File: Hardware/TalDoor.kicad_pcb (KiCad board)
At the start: 2 copper layers, 117.2 x 60.3 mm, 72 parts, among them J1 SI-52003-F_RJ45, J2 Conn_01x02, J3 Conn_01x06_Male, J4 Conn_01x06_Male, M2 Screw MountingHole_2.2mm_M2_Pad_Via, P1 PocketBeagle, Q1 RK7002BM, Q2 BSS223PWH6327XTSA1, U1 DRV8837, U2 ENC28J60-I/SO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

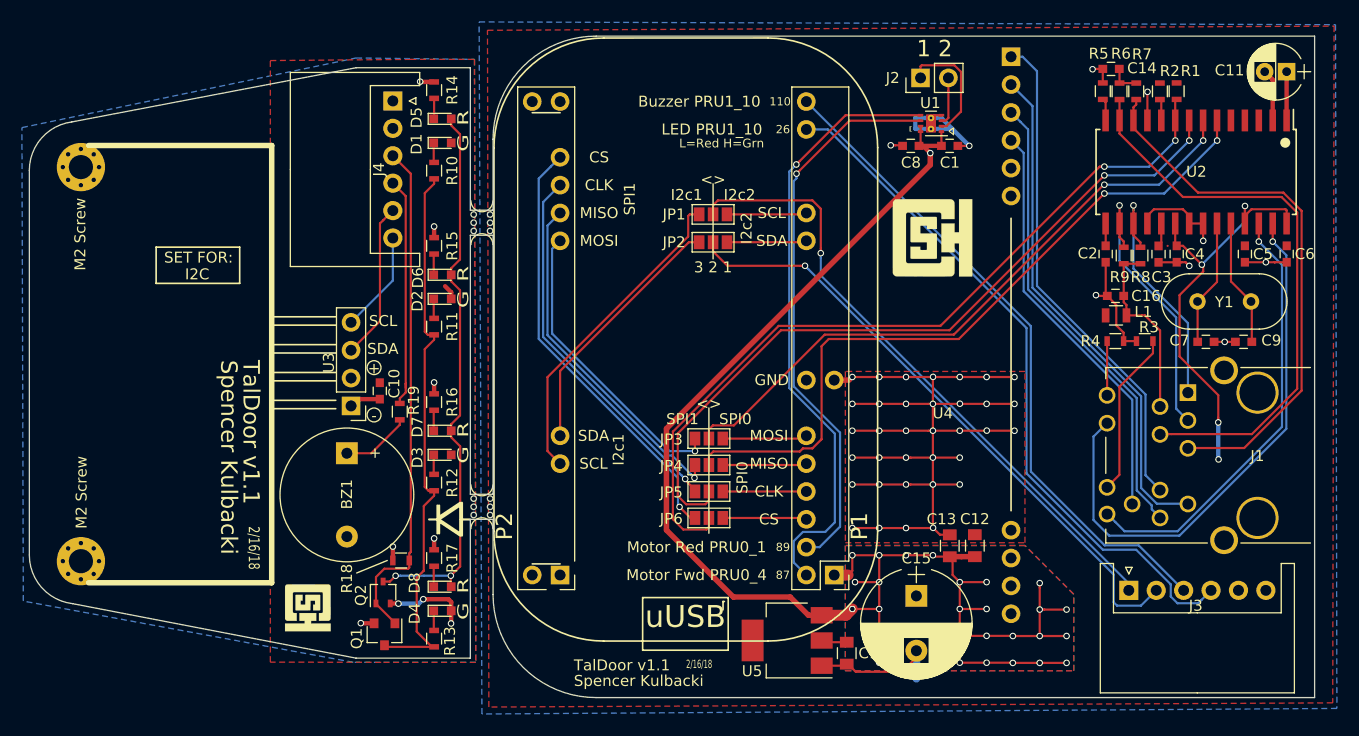
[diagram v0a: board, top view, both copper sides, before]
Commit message: updated layout to account for door mount shape issue
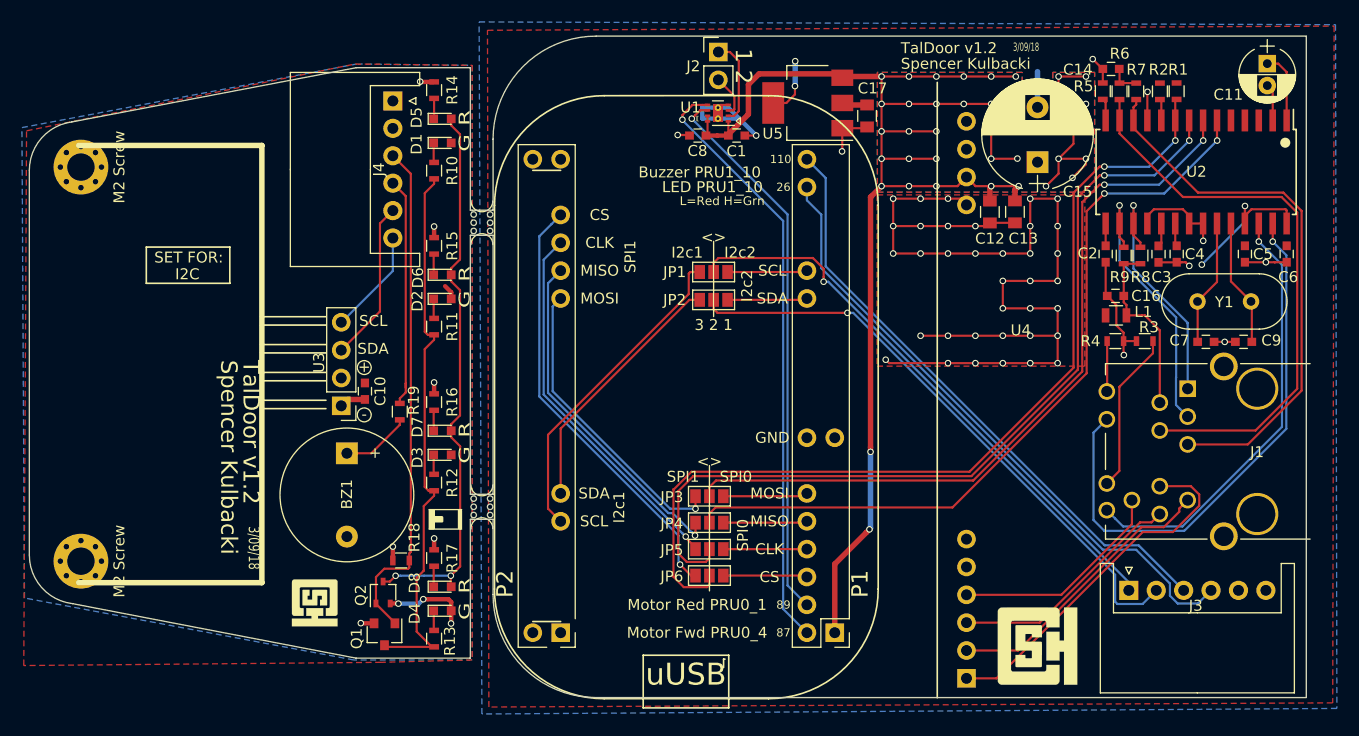
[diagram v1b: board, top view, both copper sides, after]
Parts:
- M2 Screw: footprint Mounting_Holes:MountingHole_2.2mm_M2_Pad_Via -> Mounting_Holes:MountingHole_2.5mm_Pad_Via (x2)
- moved U4 61.0 mm to (139.3, 163.5), turned to 180 degrees
- moved U5 49.1 mm to (127.5, 109.2)
- moved C17 49.0 mm to (132.9, 110.4)
- moved C15 41.1 mm to (148.5, 114.6), turned to 90 degrees
- moved G*** 38.4 mm to (148.5, 158.8)
- moved C13 31.0 mm to (146.4, 119.2), turned to 270 degrees
- moved C12 30.5 mm to (144.1, 119.2), turned to 270 degrees
- moved C8 19.5 mm to (117.5, 112.2)
- moved U1 19.5 mm to (119.3, 110.1)
- moved C1 19.5 mm to (121.0, 112.2)
- moved J2 18.6 mm to (119.4, 104.6), turned to 0 degrees
- moved JP1 5.26 mm to (118.9, 124.6)
- moved JP2 5.26 mm to (118.9, 127.2)
- moved JP3 5.26 mm to (118.5, 145.1)
- moved JP4 5.26 mm to (118.5, 147.5)
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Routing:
- net Net-(J1-Pad10): track 42.6 -> 21.7 mm
- net Net-(J1-Pad9): track 46.6 -> 26.5 mm
- net Net-(J1-Pad11): track 37.7 -> 20.0 mm
- net +3V3: track 46.0 -> 28.5 mm
- net Net-(J1-Pad8): track 45.7 -> 32.7 mm
- net /CS: track 73.2 -> 84.7 mm
- net /CLK: track 69.4 -> 80.7 mm
- net /MOSI: track 58.7 -> 69.9 mm
- net /PRU0_0: track 63.7 -> 57.3 mm
- net +5V: track 156.6 -> 163.0 mm, vias 29 -> 39
- net /MISO: track 65.9 -> 71.7 mm
- net /PRU1_10: track 60.6 -> 55.4 mm
- net /SCL: track 57.6 -> 53.2 mm
- net GND: track 151.6 -> 154.8 mm, vias 44 -> 46
- net Net-(J2-Pad1): track 11.0 -> 7.91 mm
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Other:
- board size 117.2 x 60.3 mm -> 116.5 x 60.3 mm
- board text added: "3/09/18"
- board text added: "TalDoor v1.2"
- board text removed: "2/16/18"
- board text removed: "TalDoor v1.1"

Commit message: fixed ethernet module, SPI, I2c busses
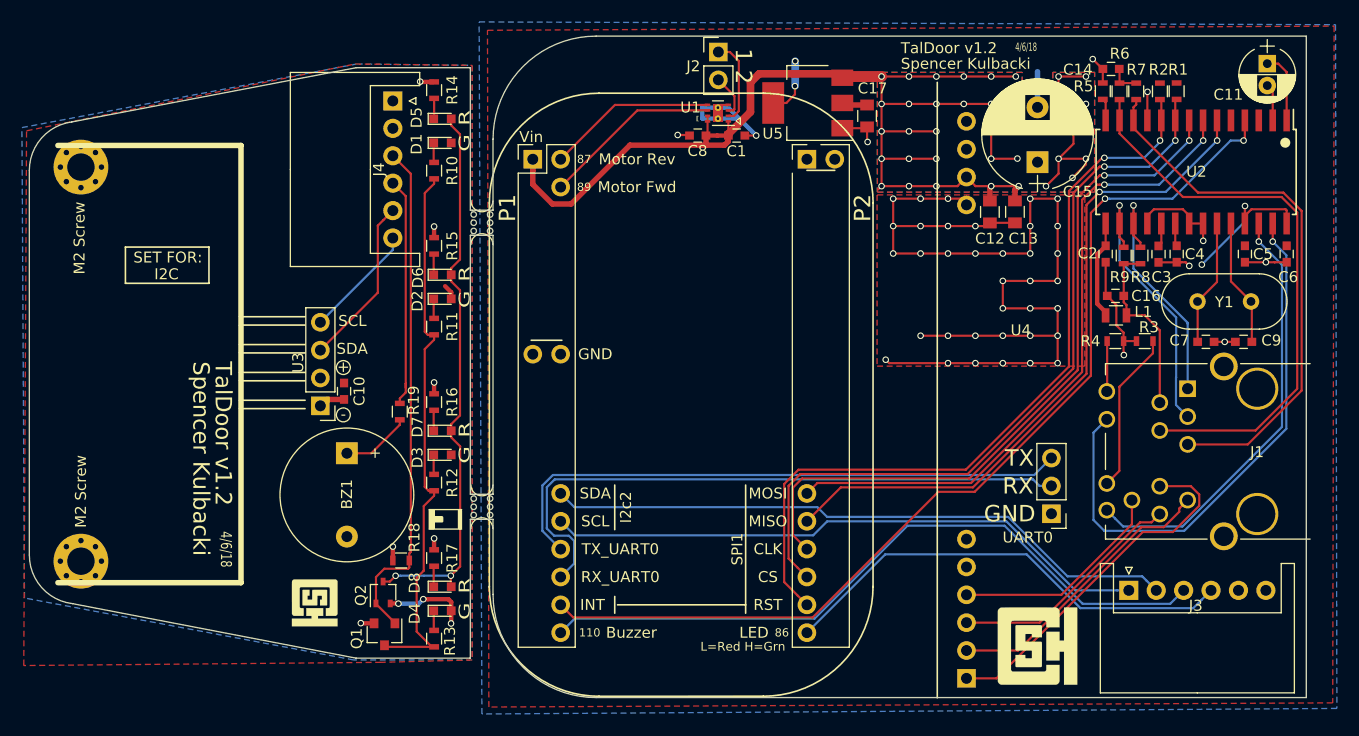
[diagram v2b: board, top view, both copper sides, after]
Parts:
- removed JP1, JP2, JP3, JP4, JP5, JP6: Jumper_NC_Dual, Connectors:GS3
- added UART0: Conn_01x03, Pin_Headers:Pin_Header_Straight_1x03_Pitch2.54mm, F.Cu at (149.7, 146.7)
- P1: footprint TalDoor_Footprints:PocketBeagle_DEV_TalDoor -> TalDoor_Footprints:PocketBeagle_TalDoor
- R19: value 150 -> 120
- moved P1 48.7 mm to (127.4, 114.4), turned to 0 degrees
- moved C10 1.91 mm to (85.2, 135.5)
- moved U3 1.90 mm to (83.1, 136.8)
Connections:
- net /PRU0_1 renamed /GPIO_87
- net /PRU0_4 renamed /GPIO_89
- net /PRU1_10 renamed /GPIO_110
- J3 pad 4: /PRU0_0 -> /GPIO_86
- P1 pad 1.26: /SDA2 -> /SDA
- P1 pad 1.28: /SCL2 -> /SCL
- P1 pad 1.34: /PRU0_0 -> /INT
- P1 pad 2.25: /MOSI2 -> /MOSI
- P1 pad 2.27: /MISO2 -> /MISO
- P1 pad 2.29: /CLK2 -> /CLK
- P1 pad 2.31: /CS2 -> /CS
- P1 pad 2.35: Net-(P1-Pad2.35) -> /GPIO_86
- R2 pad 2: Net-(R2-Pad2) -> /RST
- U2 pad 10: Net-(R2-Pad2) -> /RST
- U2 pad 4: Net-(U2-Pad4) -> /INT
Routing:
- net /INT: track 0.00 -> 91.4 mm, vias 0 -> 2
- net /RST: track 0.00 -> 72.4 mm, vias 0 -> 2
- net /PRU0_0: track 57.3 -> 0.00 mm
- net /RX_UART0: track 0.00 -> 57.1 mm
- net /TX_UART0: track 0.00 -> 54.0 mm
- net /GPIO_86: track 0.00 -> 42.5 mm
- net /CS2: track 39.8 -> 0.00 mm, vias 1 -> 0
- net /GPIO_87: track 54.6 -> 15.4 mm, vias 1 -> 0
- net /CLK2: track 34.3 -> 0.00 mm, vias 1 -> 0
- net /GPIO_89: track 50.4 -> 16.3 mm, vias 1 -> 0
- net /MISO2: track 31.6 -> 0.00 mm, vias 1 -> 0
- net /SCL1: track 29.4 -> 0.00 mm
- net /MOSI2: track 27.4 -> 0.00 mm, vias 1 -> 0
- net /SDA1: track 23.5 -> 0.00 mm
- net +5V: track 163.0 -> 145.5 mm, vias 39 -> 37
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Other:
- board text added: "4/6/18"
- board text added: "GND"
- board text added: "RX"
- board text added: "TX"
- board text removed: "3 2 1"
- board text removed: "<>"
- board text removed: "I2c1"
- board text removed: "I2c2"
- board text removed: "SPI0"
- board text removed: "SPI1"

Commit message: Updated PCB and added new photos
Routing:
- net GND: track 154.1 -> 156.4 mm, vias 46 -> 48
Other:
- board text removed: "3/09/18"
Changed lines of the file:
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@@
     (thickness 1.6)
     (drawings 165)
-    (tracks 681)
+    (tracks 685)
     (zones 0)
     (modules 67)
@@
     (pad_to_mask_clearance 0.2)
     (aux_axis_origin 0 0)
-    (visible_elements 7FFFFFFF)
+    (visible_elements 7FFFEFFF)
     (pcbplotparams
       (layerselection 0x011f0_80000001)
@@
     (effects (font (size 1.25 1.25) (thickness 0.3)))
   )
-  (gr_text "It's all about Tal" (at 150.114 105.918 180) (layer B.Mask)
+  (gr_text "It's all about Tal" (at 150.114 105.283 180) (layer B.Mask)
     (effects (font (size 1.25 1.25) (thickness 0.3)) (justify left mirror))
   )
-  (gr_text 3/09/18 (at 163.626814 155.89021 180) (layer B.SilkS)
+  (gr_text 4/6/18 (at 163.626814 155.89021 180) (layer B.SilkS)
     (effects (font (size 0.75 0.45) (thickness 0.1)) (justify mirror))
   )
@@
   (segment (start 87.70438 141.166998) (end 90.30238 138.568998) (width 0.2) (layer F.Cu) (net 1))
   (segment (start 90.30238 138.568998) (end 90.30238 138.118998) (width 0.2) (layer F.Cu) (net 1))
+  (segment (start 137.795 132.842) (end 135.001 132.842) (width 0.2) (layer F.Cu) (net 2))
+  (via (at 135.001 132.842) (size 0.6) (drill 0.4) (layers F.Cu B.Cu) (net 2))
+  (segment (start 140.298381 132.949051) (end 137.902051 132.949051) (width 0.2) (layer F.Cu) (net 2))
+  (segment (start 137.902051 132.949051) (end 137.795 132.842) (width 0.2) (layer F.Cu) (net 2))
+  (via (at 137.795 132.842) (size 0.6) (drill 0.4) (layers F.Cu B.Cu) (net 2))
+  (segment (start 137.798381 130.449051) (end 135.021051 130.449051) (width 0.2) (layer F.Cu) (net 2))
+  (segment (start 135.021051 130.449051) (end 135.001 130.429) (width 0.2) (layer F.Cu) (net 2))
+  (via (at 135.001 130.429) (size 0.6) (drill 0.4) (layers F.Cu B.Cu) (net 2))
   (segment (start 132.9182 111.4044) (end 132.9182 112.7252) (width 0.2) (layer F.Cu) (net 2))
   (segment (start 132.9182 112.7252) (end 132.969 112.776) (width 0.2) (layer F.Cu) (net 2))
   (via (at 132.969 112.776) (size 0.6) (drill 0.4) (layers F.Cu B.Cu) (net 2))
-  (segment (start 148.463 109.6175) (end 148.463 106.3625) (width 0.5) (layer B.Cu) (net 2))
+  (segment (start 148.463 109.6175) (end 148.463 106.3625) (width 1) (layer B.Cu) (net 2))
   (segment (start 153.499892 105.219002) (end 153.496628 105.219002) (width 0.2) (layer F.Cu) (net 2))
   (segment (start 154.394657 106.113767) (end 153.499892 105.219002) (width 0.2) (layer F.Cu) (net 2))
@@
   (segment (start 145.298381 130.449051) (end 142.798381 130.449051) (width 0.2) (layer F.Cu) (net 2))
   (segment (start 147.798381 130.449051) (end 145.298381 130.449051) (width 0.2) (layer F.Cu) (net 2))
-  (segment (start 134.91821 132.937669) (end 134.618211 132.63767) (width 0.2) (layer F.Cu) (net 2))
-  (segment (start 134.929592 132.949051) (end 134.91821 132.937669) (width 0.2) (layer F.Cu) (net 2))
-  (segment (start 140.298381 132.949051) (end 134.929592 132.949051) (width 0.2) (layer F.Cu) (net 2))
-  (via (at 134.618211 132.63767) (size 0.6) (drill 0.4) (layers F.Cu B.Cu) (net 2))
   (segment (start 142.798381 132.949051) (end 140.298381 132.949051) (width 0.2) (layer F.Cu) (net 2))
   (segment (start 145.298381 132.949051) (end 142.798381 132.949051) (width 0.2) (layer F.Cu) (net 2))
@@
   (segment (start 158.063461 148.35117) (end 144.718231 161.6964) (width 0.2) (layer F.Cu) (net 10))
   (segment (start 144.718231 161.6964) (end 141.986 161.6964) (width 0.2) (layer F.Cu) (net 10))
-  (segment (start 157.213657 110.811767) (end 157.213657 111.511767) (width 0.2) (layer F.Cu) (net 11))
-  (segment (start 157.213657 111.511767) (end 163.096182 117.394292) (width 0.2) (layer F.Cu) (net 11))
-  (segment (start 163.096182 117.394292) (end 170.883813 117.394292) (width 0.2) (layer F.Cu) (net 11))
+  (segment (start 157.213657 110.811767) (end 157.213657 111.907212) (width 0.2) (layer F.Cu) (net 11))
+  (segment (start 157.213657 111.907212) (end 162.700737 117.394292) (width 0.2) (layer F.Cu) (net 11))
+  (segment (start 162.700737 117.394292) (end 170.883813 117.394292) (width 0.2) (layer F.Cu) (net 11))
   (segment (start 170.883813 117.394292) (end 172.549315 119.059794) (width 0.2) (layer F.Cu) (net 11))
-  (segment (start 172.549315 119.059794) (end 172.549315 135.454199) (width 0.2) (layer F.Cu) (net 11))
   (segment (start 172.549315 135.454199) (end 167.643114 140.3604) (width 0.2) (layer F.Cu) (net 11))
+  (segment (start 172.549315 119.059794) (end 172.549315 135.454199) (width 0.2) (layer F.Cu) (net 11))
   (segment (start 167.643114 140.3604) (end 162.1536 140.3604) (width 0.2) (layer F.Cu) (net 11))
   (segment (start 157.213657 110.811767) (end 157.213657 109.611767) (width 0.2) (layer F.Cu) (net 11))
   (segment (start 157.213657 109.611767) (end 157.467657 109.357767) (width 0.2) (layer F.Cu) (net 11))
   (segment (start 157.467657 109.357767) (end 157.467657 108.907767) (width 0.2) (layer F.Cu) (net 11))
-  (segment (start 155.943657 110.811767) (end 155.943657 112.011767) (width 0.2) (layer F.Cu) (net 12))
-  (segment (start 155.943657 112.011767) (end 161.726193 117.794303) (width 0.2) (layer F.Cu) (net 12))
-  (segment (start 161.726193 117.794303) (end 170.718124 117.794303) (width 0.2) (layer F.Cu) (net 12))
+  (segment (start 155.943657 110.811767) (end 155.943657 111.896584) (width 0.2) (layer F.Cu) (net 12))
+  (segment (start 155.943657 111.896584) (end 161.841376 117.794303) (width 0.2) (layer F.Cu) (net 12))
+  (segment (start 161.841376 117.794303) (end 170.718124 117.794303) (width 0.2) (layer F.Cu) (net 12))
   (segment (start 170.718124 117.794303) (end 172.149304 119.225483) (width 0.2) (layer F.Cu) (net 12))
   (segment (start 172.149304 119.225483) (end 172.149304 135.287298) (width 0.2) (layer F.Cu) (net 12))
@@
     (polygon
       (pts
-        (xy 152.781 133.223) (xy 152.781 117.602) (xy 133.828026 117.602) (xy 133.828026 133.223)
+        (xy 152.810974 133.35) (xy 152.908 117.602) (xy 133.955026 117.602) (xy 133.858 133.35)
       )
     )

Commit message: updated BOM
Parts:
- renumbered UART0 to J5
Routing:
- net +5V: track 145.5 -> 148.7 mm
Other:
- board text added: "UART0 Debug"
- board text removed: "Old RJ45 out 3mm"
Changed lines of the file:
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@@
   (title_block
     (title "TalDoor PCB")
-    (date 2018-03-09)
+    (date 2018-04-08)
     (rev 1.2)
     (company "Spencer Kulbacki - Computer Science House")
@@
     (descr "Through hole straight pin header, 1x03, 2.54mm pitch, single row")
     (tags "Through hole pin header THT 1x03 2.54mm single row")
-    (fp_text reference UART0 (at 2.159 -2.159 180) (layer F.SilkS)
+    (fp_text reference J5 (at 0 7.239 180) (layer F.SilkS)
       (effects (font (size 1 1) (thickness 0.15)))
     )
@@
     (pad 2.35 thru_hole oval (at 0 43.18) (size 1.7 1.7) (drill 1) (layers *.Cu *.Mask)
       (net 56 /GPIO_86))
-    (pad 1.4 thru_hole oval (at -22.46 2.54) (size 1.7 1.7) (drill 1) (layers *.Cu *.Mask)
-      (net 61 /GPIO_89))
+    (pad "" np_thru_hole oval (at -22.46 5.08) (size 1.7 1.7) (drill 1) (layers *.Cu *.Mask))
     (pad 2.31 thru_hole oval (at 0 38.1) (size 1.7 1.7) (drill 1) (layers *.Cu *.Mask)
       (net 21 /CS))
@@
     (pad 1.30 thru_hole oval (at -22.46 35.56) (size 1.7 1.7) (drill 1) (layers *.Cu *.Mask)
       (net 58 /TX_UART0))
+    (pad 1.4 thru_hole oval (at -22.46 2.54) (size 1.7 1.7) (drill 1) (layers *.Cu *.Mask)
+      (net 61 /GPIO_89))
     (model ${KISYS3DMOD}/Pin_Headers.3dshapes/Pin_Header_Straight_2x18_Pitch2.54mm.wrl
       (at (xyz 0 0 0))
@@
     )
   )
+  (gr_text "UART0 Debug" (at 152.019 144.145 90) (layer F.SilkS)
+    (effects (font (size 1 1) (thickness 0.2)))
+  )
   (gr_text GND (at 145.923 146.685) (layer F.SilkS)
     (effects (font (size 1.5 1.5) (thickness 0.3)))
@@
     (effects (font (size 1.5 1.5) (thickness 0.3)))
   )
-  (gr_text "Old \nRJ45 out\n3mm " (at 205.105 145.669) (layer Dwgs.User)
-    (effects (font (size 1.5 1.5) (thickness 0.3)))
-  )
   (gr_text G (at 96.2025 112.86369 90) (layer F.SilkS)
     (effects (font (size 1 1.5) (thickness 0.2)))
@@
   (segment (start 120.819001 109.797799) (end 120.719 109.8978) (width 0.2) (layer F.Cu) (net 53))
   (segment (start 120.719 109.8978) (end 120.269 109.8978) (width 0.2) (layer F.Cu) (net 53))
-  (segment (start 118.237 113.068101) (end 111.2904 113.068101) (width 0.5) (layer F.Cu) (net 54))
-  (segment (start 111.2904 113.068101) (end 105.927691 118.43081) (width 0.5) (layer F.Cu) (net 54))
-  (segment (start 105.927691 118.43081) (end 104.221051 118.43081) (width 0.5) (layer F.Cu) (net 54))
-  (segment (start 104.221051 118.43081) (end 102.4318 116.641559) (width 0.5) (layer F.Cu) (net 54))
-  (segment (start 102.4318 116.641559) (end 102.4318 115.4008) (width 0.5) (layer F.Cu) (net 54))
+  (segment (start 118.237 113.068101) (end 113.219893 113.068101) (width 0.5) (layer F.Cu) (net 54))
+  (segment (start 113.219893 113.068101) (end 105.543686 120.744308) (width 0.5) (layer F.Cu) (net 54))
+  (segment (start 105.543686 120.744308) (end 104.404771 120.744308) (width 0.5) (layer F.Cu) (net 54))
   (segment (start 102.4318 115.4008) (end 102.4318 114.3508) (width 0.5) (layer F.Cu) (net 54))
+  (segment (start 104.404771 120.744308) (end 102.4318 118.771337) (width 0.5) (layer F.Cu) (net 54))
+  (segment (start 102.4318 118.771337) (end 102.4318 115.4008) (width 0.5) (layer F.Cu) (net 54))
   (segment (start 119.919637 113.068101) (end 118.237 113.068101) (width 0.5) (layer F.Cu) (net 54))
   (segment (start 118.225 113.056101) (end 118.237 113.068101) (width 0.2) (layer F.Cu) (net 54))
@@
       )
     )
-  )
-  (zone (net 0) (net_name "") (layer F.Cu) (hatch edge 0.508)
-    (connect_pads yes (clearance 0.2))
-    (min_thickness 0.254)
-    (keepout (tracks allowed) (vias allowed) (copperpour not_allowed))
-    (fill yes (arc_segments 16) (thermal_gap 0.508) (thermal_bridge_width 0.508))
-    (polygon
-      (pts
-        (xy 232.488611 135.509) (xy 200.992611 135.509) (xy 199.468611 137.033) (xy 199.468611 156.083) (xy 232.234611 156.083)
-      )
-    )
